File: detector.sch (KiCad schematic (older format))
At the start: 26 parts, among them J1 RF_IN_1, J2 DET_OUT_1, J3 RF_IN_2, J4 DET_OUT_2, P1 4.7k, P2 4.7k

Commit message: Switch SMA footprint from edge mount to vertical in schematic
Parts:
- J1, J2, J3, J4: footprint Connector_Coaxial:SMA_Amphenol_132289_EdgeMount -> Connector_Coaxial:SMA_Amphenol_901-144_Vertical
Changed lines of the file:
@@
 F 0 "J1" H 1130 2088 50  0000 C CNN
 F 1 "RF_IN_1" H 1130 1997 50  0000 C CNN
-F 2 "Connector_Coaxial:SMA_Amphenol_132289_EdgeMount" H 1200 1850 50  0001 C CNN
+F 2 "Connector_Coaxial:SMA_Amphenol_901-144_Vertical" H 1200 1850 50  0001 C CNN
 F 3 " ~" H 1200 1850 50  0001 C CNN
 	1    1200 1850
@@
 F 0 "J2" H 6699 1826 50  0000 L CNN
 F 1 "DET_OUT_1" H 6699 1735 50  0000 L CNN
-F 2 "Connector_Coaxial:SMA_Amphenol_132289_EdgeMount" H 6600 1850 50  0001 C CNN
+F 2 "Connector_Coaxial:SMA_Amphenol_901-144_Vertical" H 6600 1850 50  0001 C CNN
 F 3 " ~" H 6600 1850 50  0001 C CNN
 	1    6600 1850
@@
 F 0 "J3" H 1130 3538 50  0000 C CNN
 F 1 "RF_IN_2" H 1130 3447 50  0000 C CNN
-F 2 "Connector_Coaxial:SMA_Amphenol_132289_EdgeMount" H 1200 3300 50  0001 C CNN
+F 2 "Connector_Coaxial:SMA_Amphenol_901-144_Vertical" H 1200 3300 50  0001 C CNN
 F 3 " ~" H 1200 3300 50  0001 C CNN
 	1    1200 3300
@@
 F 0 "J4" H 6699 3276 50  0000 L CNN
 F 1 "DET_OUT_2" H 6699 3185 50  0000 L CNN
-F 2 "Connector_Coaxial:SMA_Amphenol_132289_EdgeMount" H 6600 3300 50  0001 C CNN
+F 2 "Connector_Coaxial:SMA_Amphenol_901-144_Vertical" H 6600 3300 50  0001 C CNN
 F 3 " ~" H 6600 3300 50  0001 C CNN
 	1    6600 3300

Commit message: Correct P2 footprint in schematic
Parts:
- P2: footprint Potentiometer_THT:Potentiometer_Bourns_3299Y_Vertical -> Potentiometer_THT:Potentiometer_Bourns_3296W_Vertical
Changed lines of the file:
@@
 F 0 "P2" H 6150 3500 50  0000 R CNN
 F 1 "4.7k" H 6200 3400 50  0000 R CNN
-F 2 "Potentiometer_THT:Potentiometer_Bourns_3299Y_Vertical" H 5950 3300 50  0001 C CNN
+F 2 "Potentiometer_THT:Potentiometer_Bourns_3296W_Vertical" H 5950 3300 50  0001 C CNN
 F 3 "~" H 5950 3300 50  0001 C CNN
 	1    5950 3300

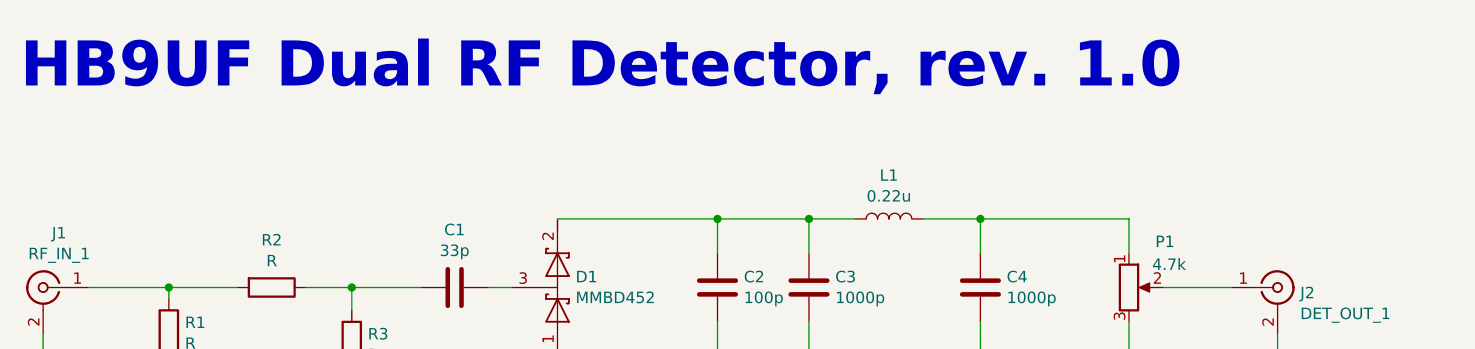
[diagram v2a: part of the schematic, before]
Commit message: Bumping revision to 1.1, put CC license on silk
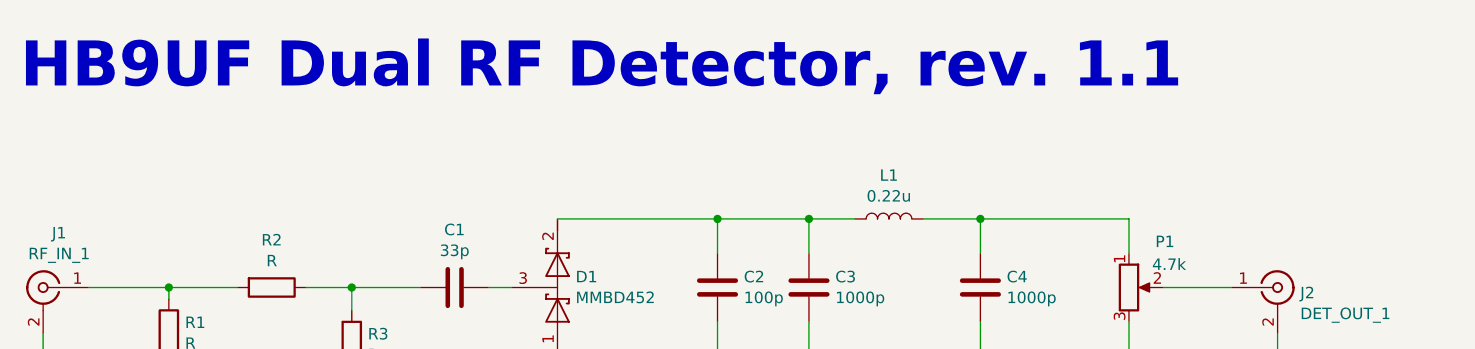
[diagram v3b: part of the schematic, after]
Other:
- note added: "HB9UF Dual RF Detector, rev. 1.1"
- note removed: "HB9UF Dual RF Detector, rev. 1.0"
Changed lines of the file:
@@
 $EndComp
 Text Notes 1100 1000 0    197  ~ 39
-HB9UF Dual RF Detector, rev. 1.0
+HB9UF Dual RF Detector, rev. 1.1
 $Comp
 L Mechanical:MountingHole_Pad H1

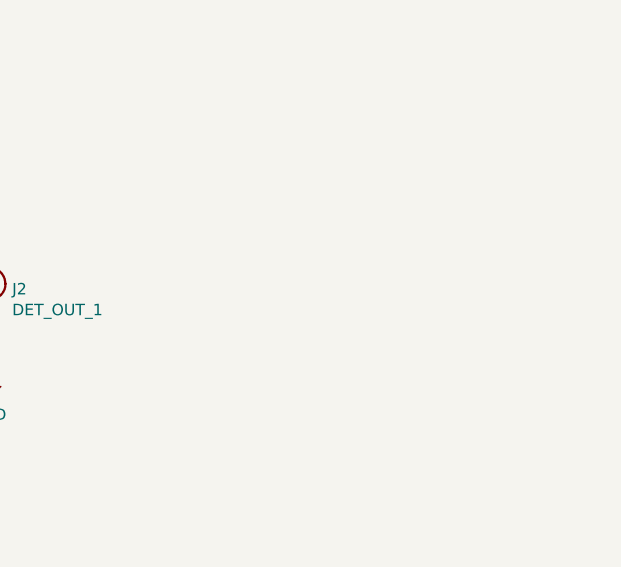
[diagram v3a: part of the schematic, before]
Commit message: Adding attenuation table for resistor values
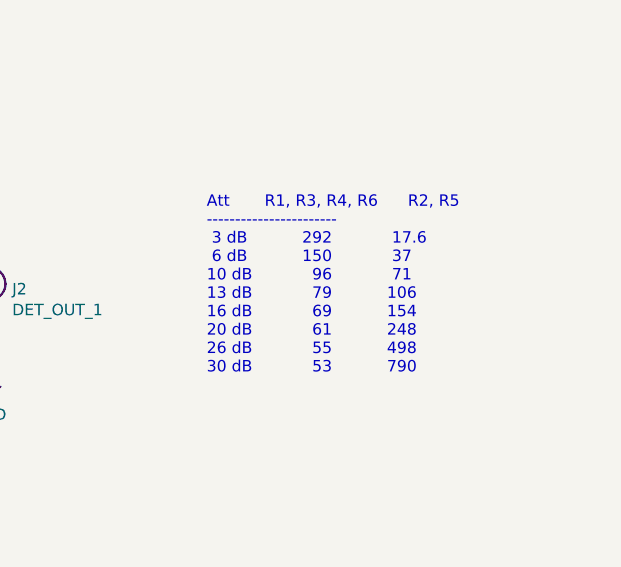
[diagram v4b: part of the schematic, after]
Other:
- note added: "Att R1, R3, R4, R6 R2, R5\n-----------------------\n 3 dB 292 17.6\n 6 dB 150 37\n10 dB 96 71\n13 dB 79 106\n16 dB 69 154\n20 dB 61 248\n26 dB 55 498\n30 dB 53 790"
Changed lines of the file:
@@
 Text Notes 2300 5000 0    50   ~ 0
 (c) Matt Weyland HB9FRV\nCC BY-SA 4.0\nBased on work by J.R. Klitzing W6PQL\nhttps://www.w6pql.com/Sampling_RF_Power.htm
+Text Notes 7550 2250 0    50   ~ 0
+Att       R1, R3, R4, R6      R2, R5\n-----------------------\n 3 dB           292            17.6\n 6 dB           150            37\n10 dB            96            71\n13 dB            79           106\n16 dB            69           154\n20 dB            61           248\n26 dB            55           498\n30 dB            53           790
 $EndSCHEMATC
